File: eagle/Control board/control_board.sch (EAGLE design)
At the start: 179 parts, among them SW1 SPST_TACT-EVQQ2, SW2 SPST_TACT-EVQQ2, U1 TCA9554A, U2 LM317, U3 LM317, U4 STM32F446, U5 TCA9554A, U6 TCA9554A, X1 JST-XH-02-PIN-LONG-PAD, X10 JST-XH-07-PIN-LONG-PAD, X11 JST-XH-07-PIN-LONG-PAD, X12 JST-XH-02-PIN-LONG-PAD, X13 JST-XH-03-PIN-LONG-PAD, X14 JST-XH-03-PIN-LONG-PAD, X15 JST-XH-08-PIN-LONG-PAD, X16 JST-XH-02-PIN-LONG-PAD, X17 JST-XH-08-PIN-LONG-PAD, X18 JST-XH-02-PIN-LONG-PAD, X2 JST-XH-06-PIN-LONG-PAD, X3 JST-XH-06-PIN-LONG-PAD, X4 JST-XH-06-PIN-LONG-PAD, X5 JST-XH-06-PIN-LONG-PAD, X6 JST-XH-06-PIN-LONG-PAD, X7 JST-XH-06-PIN-LONG-PAD, X8 JST-XH-04-PIN-LONG-PAD, X9 JST-XH-07-PIN-LONG-PAD

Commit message: Nearly done assigning gpio
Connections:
- removed net N$4: SB43.P$1
- removed net N$43: SB42.P$2
- net M1_2: now also SB19.P$1
- net M1_4: now also SB45.P$1
- net M3_1: no longer SB46.P$2
- net M3_3: no longer SB44.P$2
- net RF4_G: now also SB12.P$1; no longer SB1.P$1
- net RF5_G: now also SB13.P$1; no longer SB36.P$2
- net SW1: now also SB50.P$2
- net SW2: now also SB49.P$2
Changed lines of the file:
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@@
 <part name="R11" library="rcl" deviceset="R-US_" device="R0603" value="100"/>
 <part name="R12" library="rcl" deviceset="R-US_" device="R0603" value="100"/>
+<part name="U$27" library="custom" deviceset="NC" device=""/>
+<part name="U$34" library="custom" deviceset="NC" device=""/>
+<part name="U$35" library="custom" deviceset="NC" device=""/>
+<part name="U$36" library="custom" deviceset="NC" device=""/>
+<part name="U$38" library="custom" deviceset="NC" device=""/>
+<part name="U$39" library="custom" deviceset="NC" device=""/>
 </parts>
 <sheets>
@@
 <attribute name="DIGI" x="167.64" y="63.5" size="1.778" layer="96" rot="R180" display="off"/>
 </instance>
+<instance part="U$27" gate="G$1" x="22.86" y="180.34" rot="R180"/>
+<instance part="U$34" gate="G$1" x="160.02" y="139.7"/>
+<instance part="U$35" gate="G$1" x="22.86" y="226.06" rot="R180"/>
+<instance part="U$36" gate="G$1" x="22.86" y="220.98" rot="R180"/>
+<instance part="U$38" gate="G$1" x="22.86" y="78.74" rot="R180"/>
+<instance part="U$39" gate="G$1" x="22.86" y="205.74" rot="R180"/>
 </instances>
 <busses>
@@
 <net name="M3_1" class="0">
 <segment>
-<pinref part="SB46" gate="G$1" pin="P$2"/>
-<wire x1="160.02" y1="195.58" x2="177.8" y2="195.58" width="0.1524" layer="91"/>
-<label x="177.8" y="195.58" size="1.778" layer="95" rot="MR0"/>
-</segment>
-<segment>
 <pinref part="SB7" gate="G$1" pin="P$1"/>
 <wire x1="22.86" y1="195.58" x2="2.54" y2="195.58" width="0.1524" layer="91"/>
@@
 <net name="M3_3" class="0">
 <segment>
-<pinref part="SB44" gate="G$1" pin="P$2"/>
-<wire x1="160.02" y1="185.42" x2="177.8" y2="185.42" width="0.1524" layer="91"/>
-<label x="177.8" y="185.42" size="1.778" layer="95" rot="MR0"/>
-</segment>
-<segment>
 <pinref part="SB8" gate="G$1" pin="P$1"/>
 <wire x1="22.86" y1="190.5" x2="2.54" y2="190.5" width="0.1524" layer="91"/>
 <label x="2.54" y="190.5" size="1.778" layer="95"/>
-</segment>
-</net>
-<net name="N$43" class="0">
-<segment>
-<pinref part="SB42" gate="G$1" pin="P$2"/>
-<wire x1="160.02" y1="175.26" x2="177.8" y2="175.26" width="0.1524" layer="91"/>
-<label x="177.8" y="175.26" size="1.778" layer="95" rot="MR0"/>
 </segment>
 </net>
@@
 </segment>
 </net>
-<net name="N$4" class="0">
-<segment>
-<pinref part="SB43" gate="G$1" pin="P$1"/>
-<wire x1="160.02" y1="180.34" x2="177.8" y2="180.34" width="0.1524" layer="91"/>
-<label x="177.8" y="180.34" size="1.778" layer="95" rot="MR0"/>
-</segment>
-</net>
 <net name="M2_1" class="0">
 <segment>
@@
 </segment>
 </net>
-<net name="RF4_G" class="0">
-<segment>
-<pinref part="SB1" gate="G$1" pin="P$1"/>
-<wire x1="22.86" y1="226.06" x2="2.54" y2="226.06" width="0.1524" layer="91"/>
-<label x="2.54" y="226.06" size="1.778" layer="95"/>
-</segment>
-</net>
 <net name="RF3_G" class="0">
 <segment>
@@
 </segment>
 </net>
-<net name="RF5_G" class="0">
-<segment>
-<pinref part="SB36" gate="G$1" pin="P$2"/>
-<wire x1="160.02" y1="139.7" x2="177.8" y2="139.7" width="0.1524" layer="91"/>
-<label x="177.8" y="139.7" size="1.778" layer="95" rot="MR0"/>
-</segment>
-</net>
 <net name="M3_2" class="0">
 <segment>
@@
 </segment>
 </net>
+<net name="M1_4" class="0">
+<segment>
+<pinref part="SB45" gate="G$1" pin="P$1"/>
+<wire x1="160.02" y1="190.5" x2="177.8" y2="190.5" width="0.1524" layer="91"/>
+<label x="177.8" y="190.5" size="1.778" layer="95" rot="MR0"/>
+</segment>
+</net>
+<net name="SW1" class="0">
+<segment>
+<pinref part="SB50" gate="G$1" pin="P$2"/>
+<wire x1="160.02" y1="215.9" x2="177.8" y2="215.9" width="0.1524" layer="91"/>
+<label x="177.8" y="215.9" size="1.778" layer="95" rot="MR0"/>
+</segment>
+</net>
+<net name="SW2" class="0">
+<segment>
+<pinref part="SB49" gate="G$1" pin="P$2"/>
+<wire x1="177.8" y1="210.82" x2="160.02" y2="210.82" width="0.1524" layer="91"/>
+<label x="177.8" y="210.82" size="1.778" layer="95" rot="MR0"/>
+</segment>
+</net>
+<net name="M1_2" class="0">
+<segment>
+<pinref part="SB19" gate="G$1" pin="P$1"/>
+<wire x1="22.86" y1="129.54" x2="2.54" y2="129.54" width="0.1524" layer="91"/>
+<label x="2.54" y="129.54" size="1.778" layer="95"/>
+</segment>
+</net>
+<net name="RF4_G" class="0">
+<segment>
+<pinref part="SB12" gate="G$1" pin="P$1"/>
+<wire x1="22.86" y1="170.18" x2="2.54" y2="170.18" width="0.1524" layer="91"/>
+<label x="2.54" y="170.18" size="1.778" layer="95"/>
+</segment>
+</net>
+<net name="RF5_G" class="0">
+<segment>
+<pinref part="SB13" gate="G$1" pin="P$1"/>
+<wire x1="2.54" y1="165.1" x2="22.86" y2="165.1" width="0.1524" layer="91"/>
+<label x="2.54" y="165.1" size="1.778" layer="95"/>
+</segment>
+</net>

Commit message: Finished mapping GPIOs. Need to cross check.
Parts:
- added C8, C9: 0.1uF, rcl:C-EUC0603
- added LED5, LED6: (no value), adafruit:LEDCHIPLED_0805
- added Q1, Q2: RE1C002UN, custom:RE1C002UN
- added R13, R14: 4.7k, rcl:R-US_R0603
- added R15, R16: 100, rcl:R-US_R0603
- added R17, R18: 82, rcl:R-US_R0603
- added X19, X20: JST-XH-02-PIN-LONG-PAD, con-jst-xh:JST-XH-02-PIN-LONG-PAD
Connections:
- new net LED_DBG1: Q1.G, SB18.P$1
- new net LED_DBG1_A: LED5.A, R17.2
- new net LED_DBG1_K: LED5.C, Q1.D
- new net LED_DBG2: Q2.G, SB42.P$2
- new net LED_DBG2_A: LED6.A, R18.2
- new net LED_DBG2_K: LED6.C, Q2.D
- new net SW3: C8.2, R13.1, SB46.P$2, X19-1.S
- new net SW3_ILIM: C8.1, R15.2
- new net SW4: C9.2, R14.1, SB47.P$2, X20-1.S
- new net SW4_ILIM: C9.1, R16.2
- net GND: now also Q1.S, Q2.S, R15.1, R16.1, X19-2.S, X20-2.S
- net PP3V3: now also R13.2, R14.2, R17.1, R18.1
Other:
- note added: "Debug LEDs"

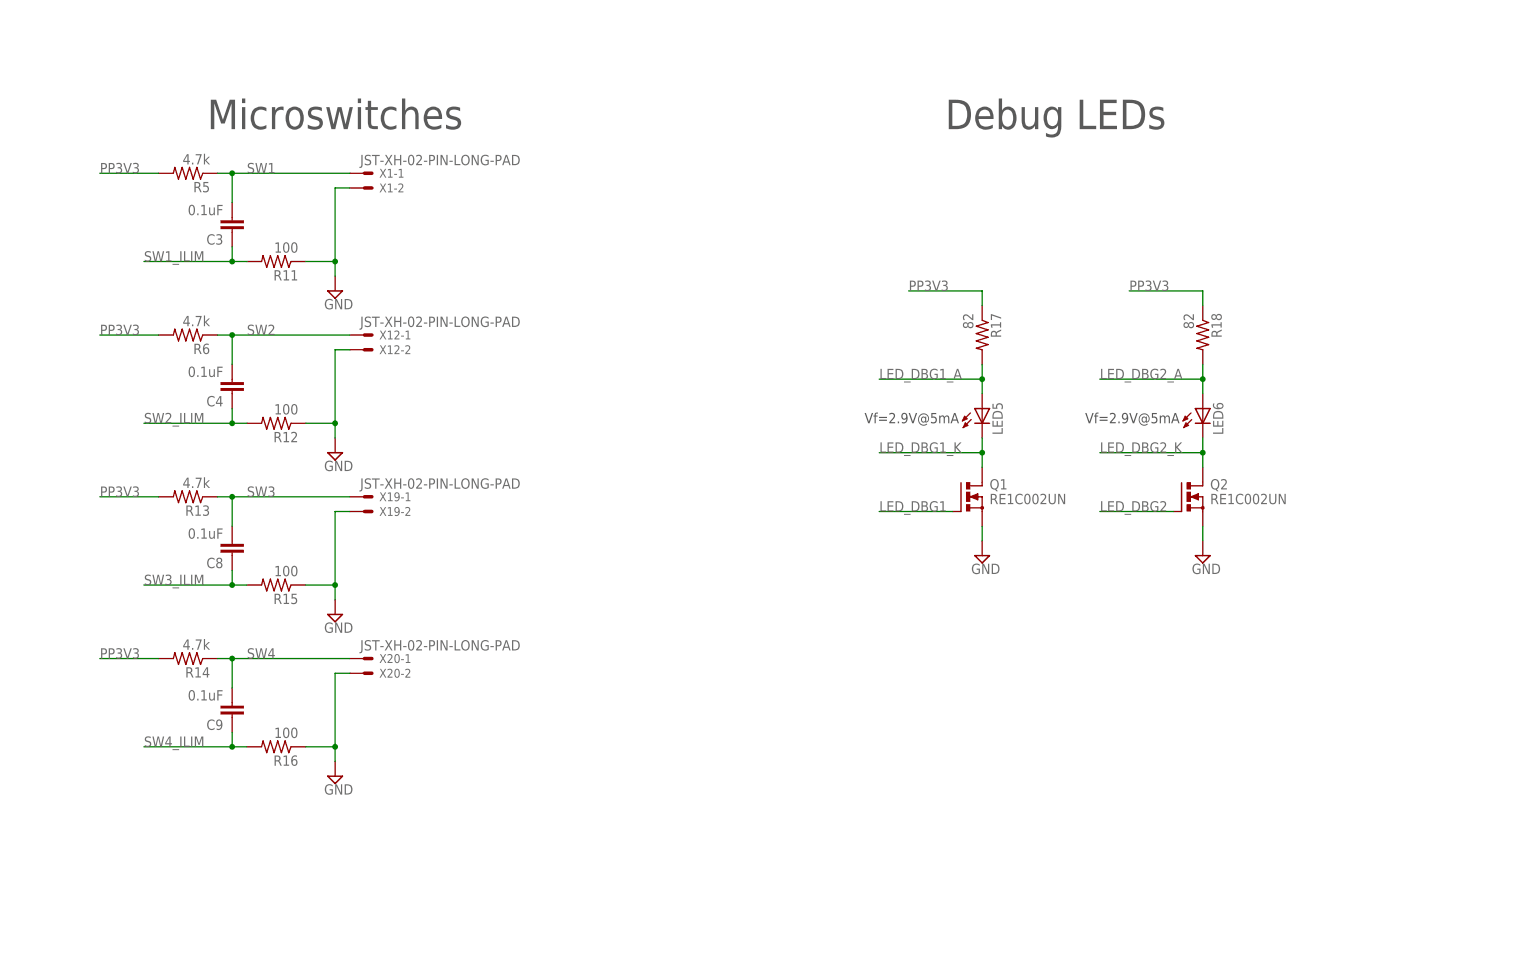
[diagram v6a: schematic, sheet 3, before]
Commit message: Added clock config to cube
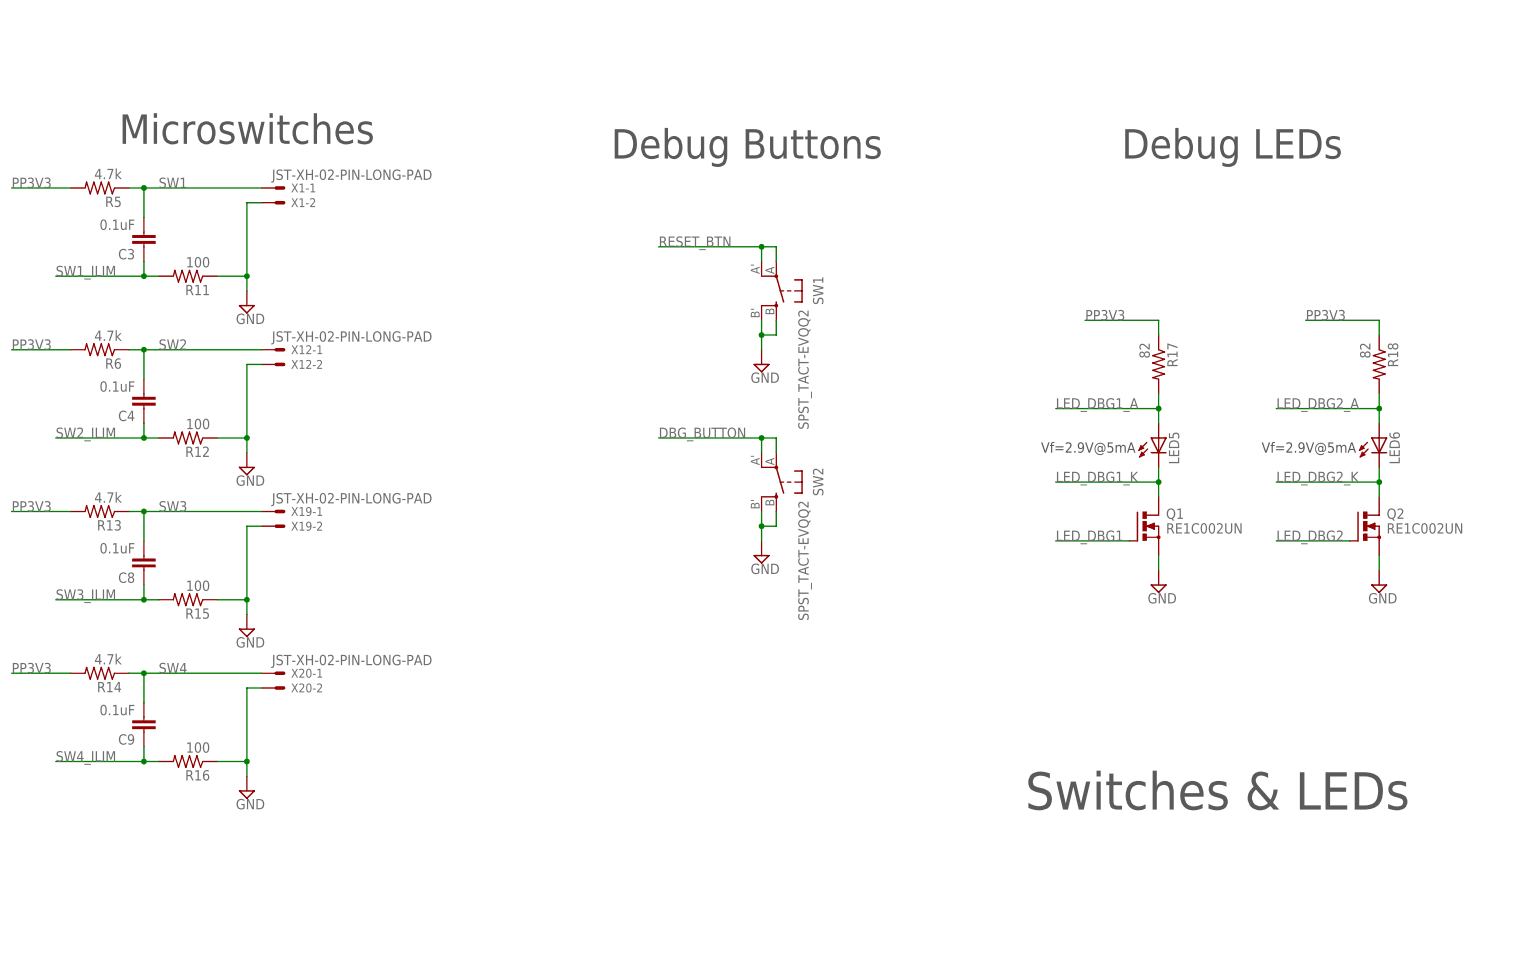
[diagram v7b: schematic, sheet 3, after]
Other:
- note added: "Debug Buttons"
- note added: "Switches & LEDs"
- moved on the sheet: C3, C4, C8, C9, LED5, LED6, Q1, Q2, R11, R12, R13, R14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

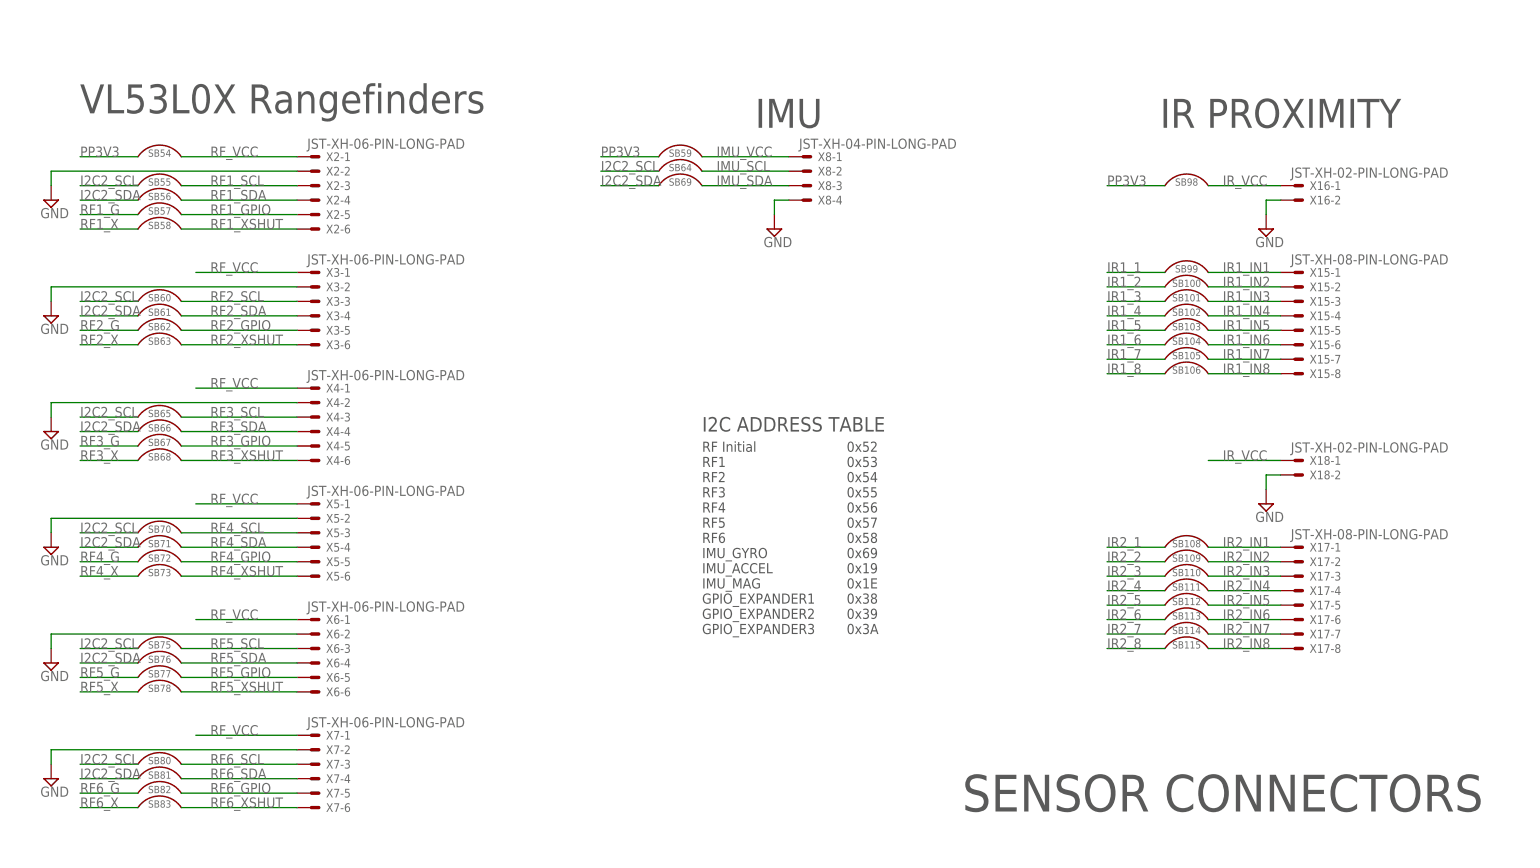
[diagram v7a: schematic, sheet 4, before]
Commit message: Added configs in Cube.
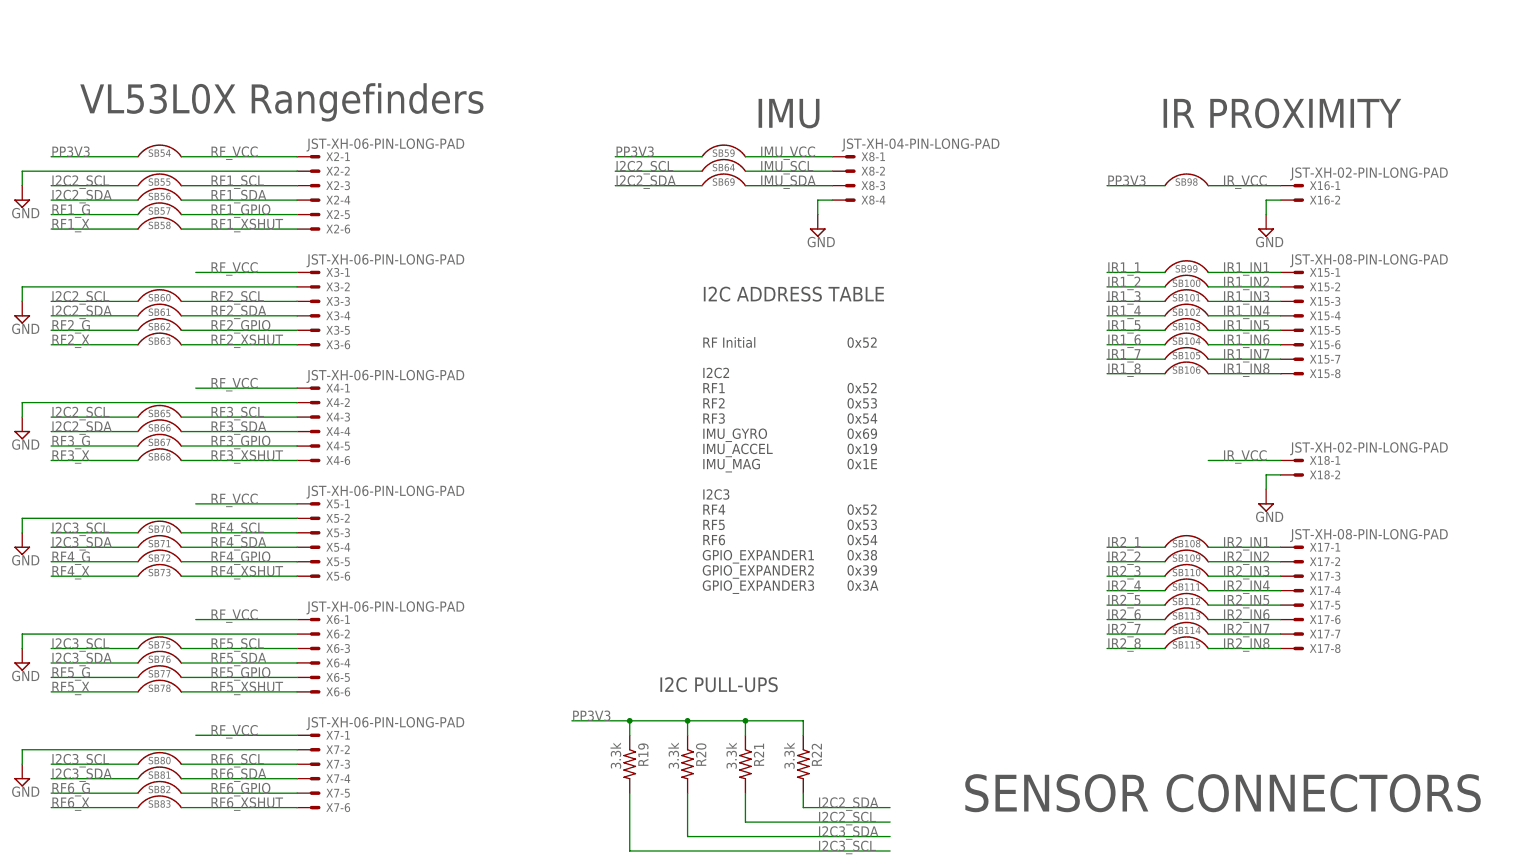
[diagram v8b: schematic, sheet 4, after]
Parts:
- added R19, R20, R21, R22: 3.3k, rcl:R-US_R0603
- added U$1, U$10, U$11, U$12, U$13, U$14, U$15, U$16, U$17, U$18, U$19, U$2, U$20, U$21, U$22, U$23, U$24, U$25, U$26, U$27, U$28, U$29, U$3, U$30, U$31, U$32, U$33, U$34, U$35, U$36, U$37, U$38, U$39, U$4, U$40, U$5, U$6, U$7, U$8, U$9: NC, custom:NC
- C1, C2: value 0.1u -> 0.1uF
- LED1: value (none) -> GREEN
- LED2, LED3, LED4, LED5, LED6: value (none) -> GREEN; DIGI (none) -> 732-4971-1-ND
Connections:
- new net N$10: U$9.P$1, U4.NC@76
- new net N$11: U$10.P$1, U4.U5V
- new net N$12: U$11.P$1, U4.E5V
- new net N$13: U$12.P$1, U4.AVDD
- new net N$14: U$13.P$1, U4.AGND
- new net N$15: U$14.P$1, U4.IOREF
- new net N$16: U$15.P$1, U4.VBAT
- new net N$17: U$16.P$1, U4.VDD
- new net N$18: U$17.P$1, U4.5V
- new net N$19: U$18.P$1, U4.3V3
- new net N$2: U$2.P$1, U4.NC@9
- new net N$20: SB1.P$1, U$35.P$1
- new net N$21: SB2.P$1, U$36.P$1
- new net N$22: SB3.P$1, U$21.P$1
- new net N$23: SB4.P$1, U$22.P$1
- new net N$24: SB5.P$1, U$39.P$1
- new net N$25: SB6.P$1, U$26.P$1
- new net N$26: SB10.P$1, U$27.P$1
- new net N$27: SB14.P$1, U$23.P$1
- new net N$28: SB15.P$1, U$24.P$1
- new net N$29: SB16.P$1, U$28.P$1
- new net N$30: SB20.P$1, U$25.P$1
- new net N$31: SB28.P$1, U$38.P$1
- new net N$32: SB35.P$2, U$32.P$1
- new net N$33: SB34.P$2, U$33.P$1
- new net N$34: SB33.P$2, U$29.P$1
- new net N$35: SB36.P$2, U$34.P$1
- new net N$36: SB37.P$2, U$20.P$1
- new net N$37: SB38.P$2, U$19.P$1
- new net N$38: SB43.P$1, U$40.P$1
- new net N$39: SB44.P$2, U$37.P$1
- new net N$4: U$3.P$1, U4.NC@10
- new net N$40: U$30.P$1, U1.INT_L
- new net N$41: U$1.P$1, U5.INT_L
- new net N$42: U$31.P$1, U6.INT_L
- new net N$5: U$4.P$1, U4.NC@11
- new net N$6: U$5.P$1, U4.NC@26
- new net N$7: U$6.P$1, U4.NC@48
- new net N$8: U$7.P$1, U4.NC@56
- new net N$9: U$8.P$1, U4.NC@74
- net I2C2_SCL: now also R21.2; no longer SB116.P$1, SB118.P$1, SB120.P$1, SB70.P$1, SB75.P$1, SB80.P$1
- net I2C2_SDA: now also R22.2; no longer SB107.P$1, SB117.P$1, SB119.P$1, SB71.P$1, SB76.P$1, SB81.P$1
- net I2C3_SCL: now also R19.2, SB116.P$1, SB118.P$1, SB120.P$1, SB70.P$1, SB75.P$1, SB80.P$1
- net I2C3_SDA: now also R20.2, SB107.P$1, SB117.P$1, SB119.P$1, SB71.P$1, SB76.P$1, SB81.P$1
- net PP3V3: now also R19.1, R20.1, R21.1, R22.1
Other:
- note added: "0x52 0x52 0x53 0x54 0x69 0x19 0x1E 0x52 0x53 0x54 0x38 0x39 0x3A"
- note added: "I2C PULL-UPS"
- note added: "RF Initial I2C2 RF1 RF2 RF3 IMU_GYRO IMU_ACCEL IMU_MAG I2C3 RF4 RF5 RF6 GPIO_EXPANDER1 GPIO_EXPANDER2 GPIO_EXPANDER3"
- note removed: "0x52 0x53 0x54 0x55 0x56 0x57 0x58 0x69 0x19 0x1E 0x38 0x39 0x3A"
- note removed: "RF Initial RF1 RF2 RF3 RF4 RF5 RF6 IMU_GYRO IMU_ACCEL IMU_MAG GPIO_EXPANDER1 GPIO_EXPANDER2 GPIO_EXPANDER3"
- moved on the sheet: C5, SB107, SB116, SB59, SB64, SB69, U1, X8-1, X8-2, X8-3, X8-4
